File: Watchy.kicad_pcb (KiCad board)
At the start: 2 copper layers, 33.8 x 46 mm, 57 parts, among them J1 FPC24(0.5MM), J2 Micro USB, J3 Battery, M1 Vibration_Motor, Q1 AO3400A, Q2 UMH3N, Q4 CJ2301, Q5 S8050, SW1 BTN, SW2 BTN, SW3 BTN, SW4 BTN, U1 ESP32-PICO-D4, U2 ME6211C33M5G-N, U3 CP2104, U4 BMA423, U5 TP4054, U6 DS3231MZ

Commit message: added body step & STL
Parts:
- moved REF** 0.55 mm to (85.6, 93.2)

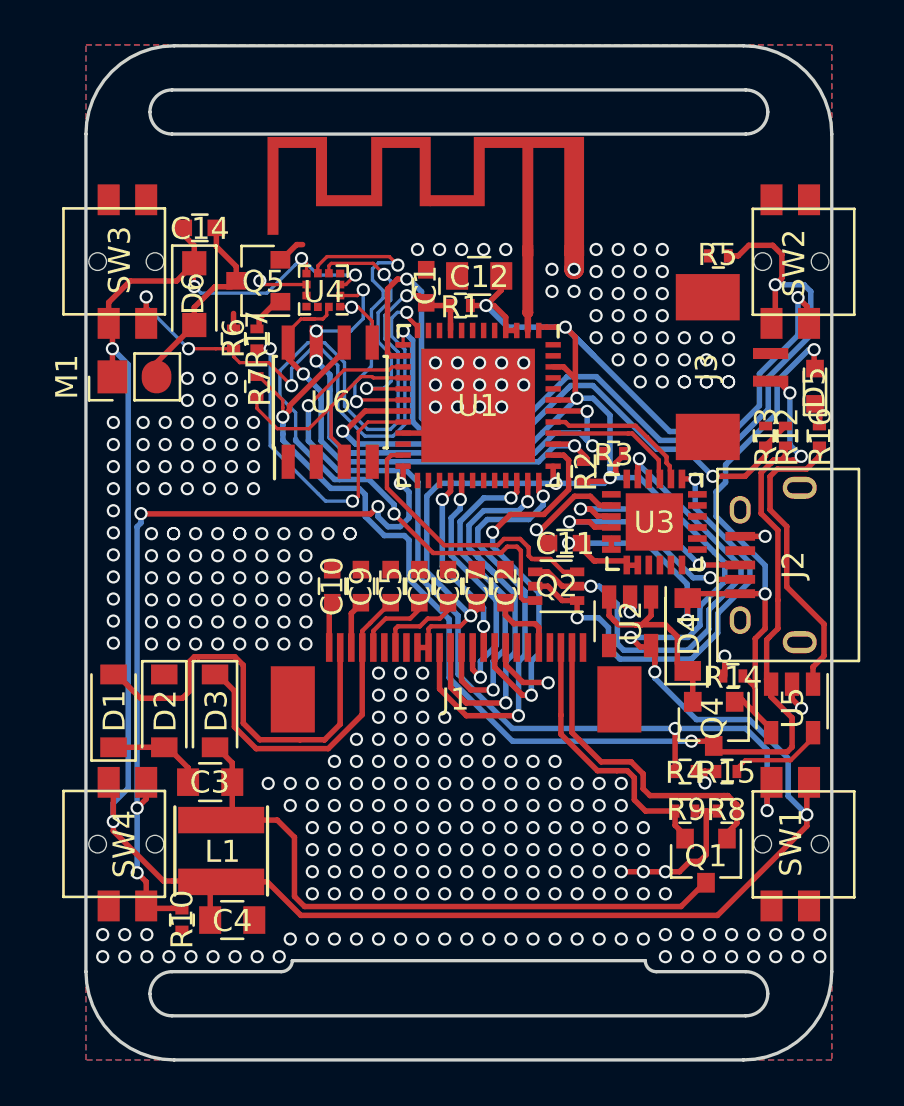
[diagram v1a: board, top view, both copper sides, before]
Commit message: added testpoints
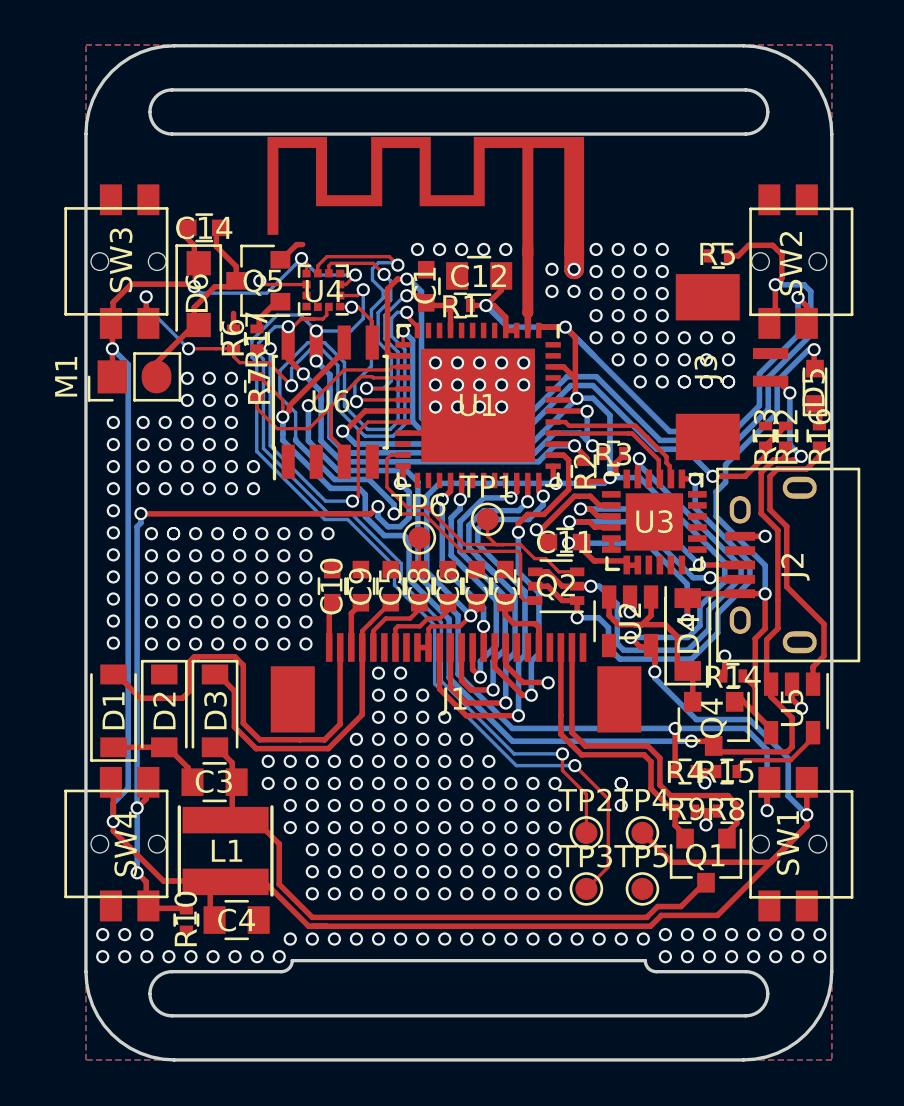
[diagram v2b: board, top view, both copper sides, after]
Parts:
- added TP1: GPIO0, TestPoint:TestPoint_Pad_D1.0mm, F.Cu at (86.9, 91.6)
- added TP2: SCL, TestPoint:TestPoint_Pad_D1.0mm, F.Cu at (91.4, 105.8)
- added TP3: SDA, TestPoint:TestPoint_Pad_D1.0mm, F.Cu at (91.4, 108.4)
- added TP4: 3V3, TestPoint:TestPoint_Pad_D1.0mm, F.Cu at (93.9, 105.8)
- added TP5: GND, TestPoint:TestPoint_Pad_D1.0mm, F.Cu at (93.9, 108.4)
- added TP6: GND, TestPoint:TestPoint_Pad_D1.0mm, F.Cu at (83.8, 92.5)
- moved C14 0.20 mm to (74.1, 78.4)
- moved C3 0.20 mm to (74.5, 103.5)
- moved C4 0.20 mm to (75.5, 109.8)
- moved D6 0.20 mm to (73.8, 81.4)
- moved L1 0.20 mm to (75.0, 106.6)
- moved R10 0.20 mm to (73.2, 109.8)
- moved SW1 0.10 mm to (100.6, 106.3)
- moved SW2 0.10 mm to (100.6, 79.9)
- moved SW3 0.10 mm to (70.6, 79.9)
- moved SW4 0.10 mm to (70.6, 106.3)
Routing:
- net SDA: track 27.9 -> 65.7 mm, vias 5 -> 6
- net SCL: track 22.9 -> 55.5 mm, vias 2 -> 4
- net +3V3: track 187.0 -> 196.2 mm
- net GND: track 31.9 -> 27.9 mm, vias 333 -> 308
- net Net-(C3-Pad2): track 29.1 -> 30.2 mm
- net BUSY: track 18.8 -> 17.9 mm
- net GPIO0: track 13.4 -> 14.0 mm

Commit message: v1.5
- switched to new RTC (PCF8563)
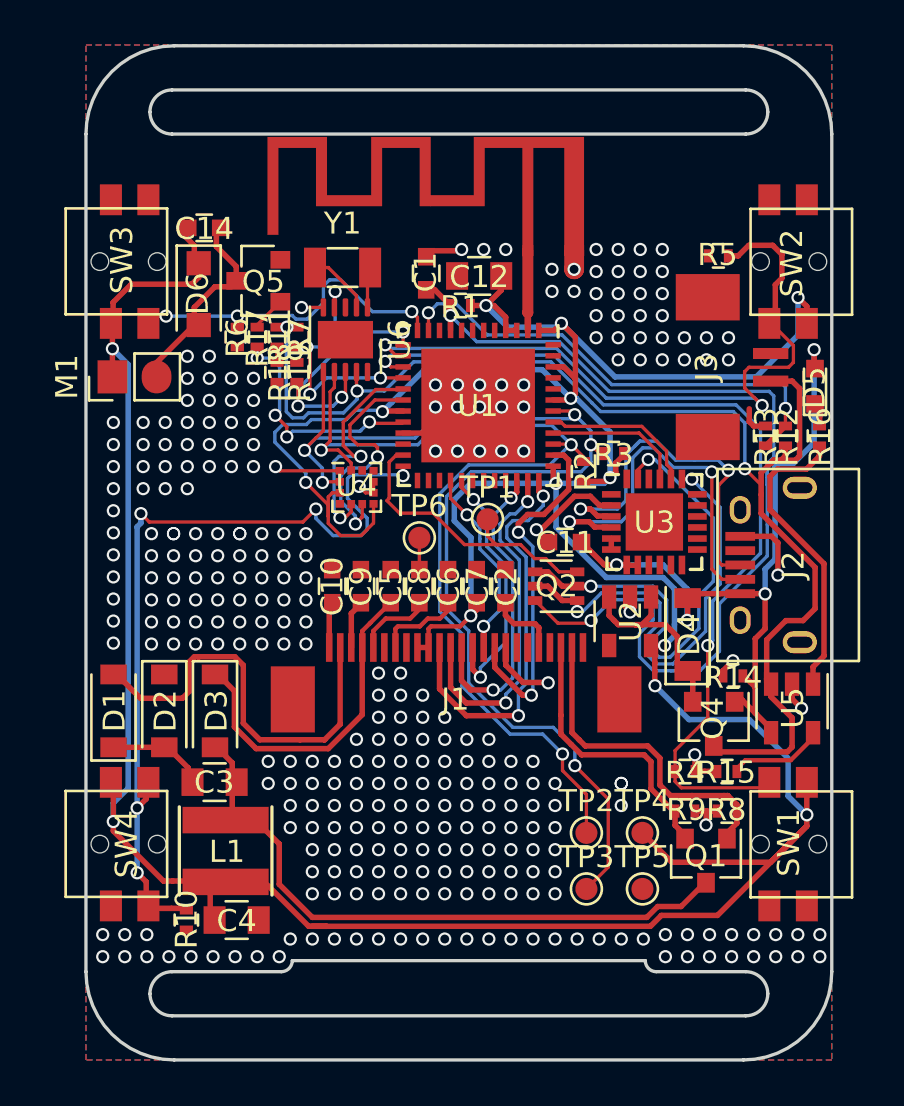
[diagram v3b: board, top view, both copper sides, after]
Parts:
- added R11: 680K, Watchy:R_0402, F.Cu at (77.4, 83.3)
- added R18: 220K, Watchy:R_0402, F.Cu at (77.4, 85.0)
- added R19: 100K, Watchy:R_0402, F.Cu at (78.3, 85.0)
- added Y1: 32.768KHz, Crystal:Crystal_SMD_3215-2Pin_3.2x1.5mm, F.Cu at (80.3, 80.2)
- U6: value DS3231MZ -> PCF8563BS; footprint Housings_SOIC:SOIC-8_3.9x4.9mm_Pitch1.27mm -> Package_DFN_QFN:DFN-10-1EP_3x3mm_P0.5mm_EP1.7x2.5mm
- moved U4 9.07 mm to (81.0, 90.2), turned to 0 degrees
- moved U6 2.91 mm to (80.5, 83.5), turned to 270 degrees
- moved R7 2.88 mm to (78.3, 83.3)
- moved G*** 1.50 mm to (75.6, 81.0)
- moved C1 0.59 mm to (84.1, 80.5)
- moved R6 0.19 mm to (75.6, 83.3), turned to 90 degrees
- moved R17 0.08 mm to (76.5, 83.3)
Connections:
- U1 pad 11: Net-(U1-Pad11) -> ADC
- U1 pad 13: ADC -> 32KHZ
- U6 pad 2: GND -> Net-(U6-Pad2)
- U6 pad 3: RTC_INT -> Net-(U6-Pad3)
- U6 pad 4: Net-(U6-Pad4) -> RTC_INT
- U6 pad 6: +BATT -> SDA
- U6 pad 7: SDA -> SCL
- U6 pad 8: SCL -> 32KHZ
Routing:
- net SDA: track 65.7 -> 53.2 mm, vias 6 -> 5
- net BTN_2: track 43.2 -> 31.2 mm
- net 32KHZ: track 0.00 -> 11.9 mm, vias 0 -> 3
- net BTN_3: track 26.0 -> 15.4 mm, vias 4 -> 3
- net SCL: track 55.5 -> 45.6 mm, vias 4 -> 3
- net EN: track 37.7 -> 45.9 mm
- net Net-(J2-Pad3): track 9.60 -> 16.7 mm
- net +3V3: track 196.2 -> 189.4 mm, vias 16 -> 14
- net Net-(J2-Pad2): track 10.6 -> 17.4 mm
- net VBUS: track 39.3 -> 34.6 mm
- net VIB_PWM: track 15.8 -> 11.2 mm, vias 2 -> 4
- net ADC: track 26.0 -> 21.8 mm
- net ACC_INT_2: track 14.5 -> 10.9 mm
- net GND: track 27.9 -> 30.8 mm, vias 308 -> 305
- net +BATT: track 62.5 -> 59.5 mm, vias 4 -> 3
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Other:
- board text added: "+"
- board text added: "-"
- board text added: "SQFMI"

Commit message: v2.0
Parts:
- added C13: 4.7uF, Capacitor_SMD:C_0402_1005Metric, F.Cu at (90.0, 91.9)
- added G***: LOGO, Watchy:sqfmi_duck, F.Cu at (85.6, 106.4)
- added R20: 100K, Watchy:R_0402, F.Cu at (84.8, 91.4)
- C1, C10, C14, C2, C5, C6, C7, C8, C9: footprint Capacitors_SMD:C_0603 -> Capacitor_SMD:C_0603_1608Metric
- C11: value 100nF -> 4.7uF; footprint Capacitors_SMD:C_0603 -> Capacitor_SMD:C_0402_1005Metric
- U3: value CP2104 -> CP2102
- moved TP6 1.00 mm to (82.8, 92.2)
- moved C11 0.46 mm to (90.0, 92.8)
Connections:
- U1 pad 10: Net-(U1-Pad10) -> ADC
- U1 pad 11: ADC -> BTN_3
- U1 pad 12: BTN_3 -> Net-(U1-Pad12)
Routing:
- net ADC: track 21.8 -> 24.6 mm
- net Net-(C13-Pad1): track 0.45 -> 2.97 mm
- net +3V3: track 189.4 -> 191.4 mm, vias 14 -> 15
- net Net-(J2-Pad2): track 17.4 -> 15.4 mm
- net BUSY: track 17.2 -> 18.8 mm
- net RES: track 8.78 -> 9.55 mm
- net VBUS: track 34.6 -> 35.2 mm
- net GND: track 30.8 -> 30.5 mm, vias 305 -> 275
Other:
- board text added: "WATCHY"
